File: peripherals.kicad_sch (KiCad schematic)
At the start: 23 parts, among them CN1 PJ-3059-B, CN2 PJ-3059-B, SW3 K2-1808SN-A4SW, SW4 K2-1808SN-A4SW, U48 2.54-1*4, U49 2.54-1*4, U50 LMV358IDR

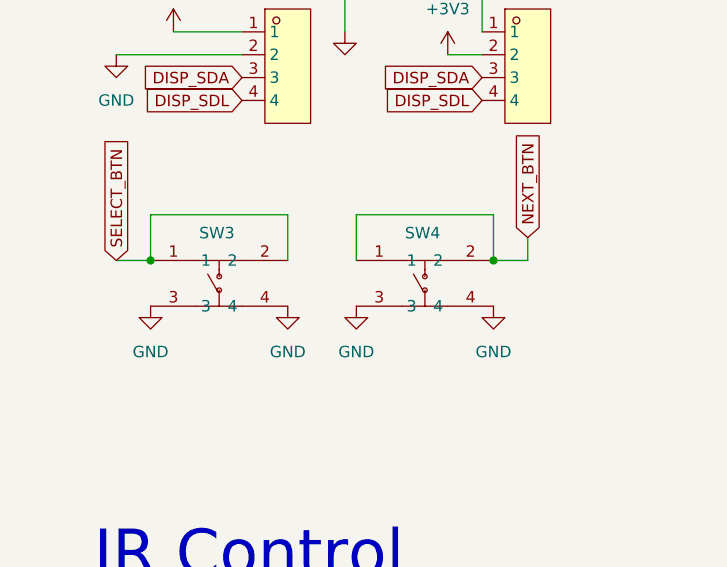
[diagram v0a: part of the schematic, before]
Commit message: Library shuffle and Fabrication Toolkit micro adjustments
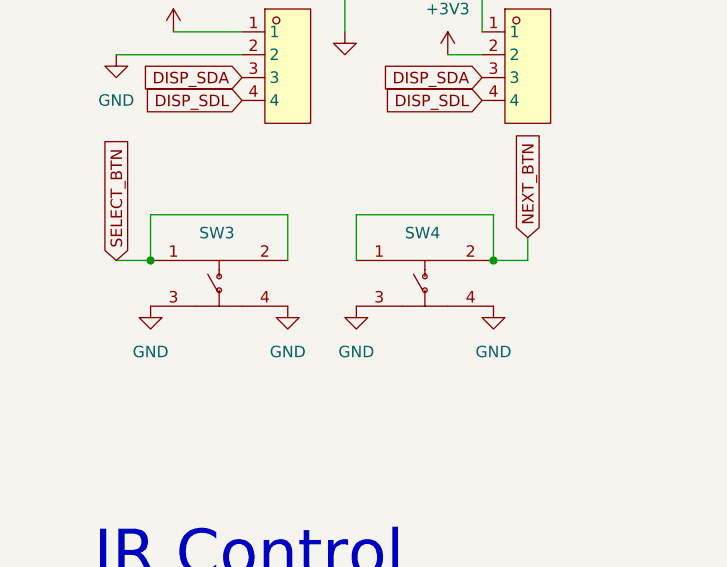
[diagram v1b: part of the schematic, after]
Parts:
- C43: footprint PCM_JLCPCB:C_0402 -> PixelBlit:C_0402; symbol PCM_JLCPCB-Capacitors:0402,1uF -> PixelBlit:0402,1uF
- C44: footprint PCM_JLCPCB:C_0402 -> PixelBlit:C_0402; symbol PCM_JLCPCB-Capacitors:0402,100nF -> PixelBlit:0402,100nF
- C45: footprint PCM_JLCPCB:C_0402 -> PixelBlit:C_0402; symbol PCM_JLCPCB-Capacitors:0402,4.7uF -> PixelBlit:0402,4.7uF
- CN1, CN2: footprint EasyEDA:AUDIO-TH_XKB_PJ-3059-B -> PixelBlit:AUDIO-TH_XKB_PJ-3059-B; symbol EasyEDA:PJ-3059-B -> PixelBlit:PJ-3059-B
- Card1: footprint EasyEDA:TF-SMD_TF-PUSH -> PixelBlit:TF-SMD_TF-PUSH; symbol EasyEDA:TFPUSH -> PixelBlit:TFPUSH
- D4, D5: footprint PCM_JLCPCB:D_SMA -> PixelBlit:D_SMA; symbol PCM_JLCPCB-Diodes:Schottky,SS14 -> PixelBlit:Schottky,SS14
- D6: footprint PCM_JLCPCB:D_0603 -> PixelBlit:D_0603; symbol PCM_JLCPCB-Diodes:LED,0603,Red -> PixelBlit:LED,0603,Red
- R57, R58, R59: footprint PCM_JLCPCB:R_0402 -> PixelBlit:R_0402; symbol PCM_JLCPCB-Resistors:0402,47kΩ -> PixelBlit:0402,47kΩ
- R60, R61: footprint PCM_JLCPCB:R_0603 -> PixelBlit:R_0603; symbol PCM_JLCPCB-Resistors:0603,1kΩ -> PixelBlit:0603,1kΩ
- R62: footprint EasyEDA:RES-ADJ-TH_3362P -> PixelBlit:RES-ADJ-TH_3362P; symbol EasyEDA:3362P-1-503LF -> PixelBlit:3362P-1-503LF
- R65: footprint PCM_JLCPCB:R_0402 -> PixelBlit:R_0402; symbol PCM_JLCPCB-Resistors:0402,1kΩ -> PixelBlit:0402,1kΩ
- R66: footprint PCM_JLCPCB:R_0402 -> PixelBlit:R_0402; symbol PCM_JLCPCB-Resistors:0402,1kΩ -> PixelBlit:0402,1kΩ_1
- R67: footprint PCM_JLCPCB:R_0402 -> PixelBlit:R_0402; symbol PCM_JLCPCB-Resistors:0402,470kΩ -> PixelBlit:0402,470kΩ
- SW3, SW4: footprint EasyEDA:KEY-SMD_4P-L4.2-W3.2-P2.20-LS5.1-TL -> PixelBlit:KEY-SMD_4P-L4.2-W3.2-P2.20-LS5.1-TL; symbol EasyEDA:K2-1808SN-A4SW -> PixelBlit:K2-1808SN-A4SW
- U48, U49: footprint EasyEDA:HDR-TH_4P-P2.54-V-M-1 -> PixelBlit:HDR-TH_4P-P2.54-V-M-1; symbol EasyEDA:2.54-1*4 -> PixelBlit:2.54-1*4
- U50: footprint EasyEDA:SOIC-8_L4.9-W3.9-P1.27-LS6.0-BL -> PixelBlit:SOIC-8_L4.9-W3.9-P1.27-LS6.0-BL; symbol EasyEDA:LMV358IDR -> PixelBlit:LMV358IDR
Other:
- moved on the sheet: SW3, SW4
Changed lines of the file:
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@@
 	)
 	(symbol
-		(lib_id "power:GND")
+		(lib_id "PixelBlit:GND")
 		(at 67.31 66.04 0)
 		(unit 1)
@@
 	)
 	(symbol
-		(lib_id "power:GND")
+		(lib_id "PixelBlit:GND")
 		(at 180.34 146.05 0)
 		(unit 1)
@@
 	)
 	(symbol
-		(lib_id "PCM_JLCPCB-Diodes:Schottky,SS14")
+		(lib_id "PixelBlit:Schottky,SS14")
 		(at 125.73 123.19 180)
 		(unit 1)
@@
 			)
 		)
-		(property "Footprint" "PCM_JLCPCB:D_SMA"
+		(property "Footprint" "PixelBlit:D_SMA"
 			(at 127.508 123.19 90)
 			(effects
@@
 	)
 	(symbol
-		(lib_id "EasyEDA:PJ-3059-B")
+		(lib_id "PixelBlit:PJ-3059-B")
 		(at 138.43 101.6 0)
 		(unit 1)
@@
 			)
 		)
-		(property "Footprint" "EasyEDA:AUDIO-TH_XKB_PJ-3059-B"
+		(property "Footprint" "PixelBlit:AUDIO-TH_XKB_PJ-3059-B"
 			(at 138.43 114.3 0)
 			(effects
@@
 	)
 	(symbol
-		(lib_id "power:GND")
+		(lib_id "PixelBlit:GND")
 		(at 54.61 119.38 0)
 		(unit 1)
@@
 	)
 	(symbol
-		(lib_id "power:GND")
+		(lib_id "PixelBlit:GND")
 		(at 44.45 66.04 0)
 		(unit 1)
@@
 	)
 	(symbol
-		(lib_id "power:GND")
+		(lib_id "PixelBlit:GND")
 		(at 82.55 66.04 0)
 		(unit 1)
@@
 	)
 	(symbol
-		(lib_id "power:GND")
+		(lib_id "PixelBlit:GND")
 		(at 40.64 38.1 0)
 		(unit 1)
@@
 	)
 	(symbol
-		(lib_id "PCM_JLCPCB-Resistors:0402,47kΩ")
+		(lib_id "PixelBlit:0402,47kΩ")
 		(at 175.26 30.48 0)
 		(unit 1)
@@
 			)
 		)
-		(property "Footprint" "PCM_JLCPCB:R_0402"
+		(property "Footprint" "PixelBlit:R_0402"
 			(at 173.482 30.48 90)
 			(effects
@@
 	)
 	(symbol
-		(lib_id "PCM_JLCPCB-Resistors:0402,47kΩ")
+		(lib_id "PixelBlit:0402,47kΩ")
 		(at 175.26 45.72 0)
 		(unit 1)
@@
 			)
 		)
-		(property "Footprint" "PCM_JLCPCB:R_0402"
+		(property "Footprint" "PixelBlit:R_0402"
 			(at 173.482 45.72 90)
 			(effects
@@
 	)
 	(symbol
-		(lib_id "EasyEDA:K2-1808SN-A4SW")
+		(lib_id "PixelBlit:K2-1808SN-A4SW")
 		(at 74.93 63.5 0)
 		(unit 1)
@@
 			)
 		)
-		(property "Footprint" "EasyEDA:KEY-SMD_4P-L4.2-W3.2-P2.20-LS5.1-TL"
+		(property "Footprint" "PixelBlit:KEY-SMD_4P-L4.2-W3.2-P2.20-LS5.1-TL"
 			(at 74.93 73.66 0)
 			(effects
@@
 	)
 	(symbol
-		(lib_id "power:+3V3")
+		(lib_id "PixelBlit:+3V3")
 		(at 46.99 35.56 0)
 		(unit 1)
@@
 	)
 	(symbol
-		(lib_id "PCM_JLCPCB-Resistors:0603,1kΩ")
+		(lib_id "PixelBlit:0603,1kΩ")
 		(at 193.04 96.52 180)
 		(unit 1)
@@
 			)
 		)
-		(property "Footprint" "PCM_JLCPCB:R_0603"
+		(property "Footprint" "PixelBlit:R_0603"
 			(at 194.818 96.52 90)
 			(effects
@@
 	)
 	(symbol
-		(lib_id "PCM_JLCPCB-Resistors:0402,1kΩ")
+		(lib_id "PixelBlit:0402,1kΩ")
 		(at 212.09 128.27 270)
 		(unit 1)
@@
 			)
 		)
-		(property "Footprint" "PCM_JLCPCB:R_0402"
+		(property "Footprint" "PixelBlit:R_0402"
 			(at 212.09 126.492 90)
 			(effects
@@
 	(symbol
 		(lib_name "0402,1kΩ_1")
-		(lib_id "PCM_JLCPCB-Resistors:0402,1kΩ")
+		(lib_id "PixelBlit:0402,1kΩ_1")
 		(at 158.75 119.38 0)
 		(unit 1)
@@
 			)
 		)
-		(property "Footprint" "PCM_JLCPCB:R_0402"
+		(property "Footprint" "PixelBlit:R_0402"
 			(at 156.972 119.38 90)
 			(effects
@@
 	)
 	(symbol
-		(lib_id "PCM_JLCPCB-Diodes:LED,0603,Red")
+		(lib_id "PixelBlit:LED,0603,Red")
 		(at 222.25 128.27 90)
 		(unit 1)
@@
 			)
 		)
-		(property "Footprint" "PCM_JLCPCB:D_0603"
+		(property "Footprint" "PixelBlit:D_0603"
 			(at 222.25 130.048 90)
 			(effects
@@
 	)
 	(symbol
-		(lib_id "PCM_JLCPCB-Capacitors:0402,4.7uF")
+		(lib_id "PixelBlit:0402,4.7uF")
 		(at 240.03 121.92 0)
 		(unit 1)
@@
 			)
 		)
-		(property "Footprint" "PCM_JLCPCB:C_0402"
+		(property "Footprint" "PixelBlit:C_0402"
 			(at 238.252 121.92 90)
 			(effects
@@
 	)
 	(symbol
-		(lib_id "power:+5V")
+		(lib_id "PixelBlit:+5V")
 		(at 54.61 105.41 0)
 		(unit 1)
@@
 	)
 	(symbol
-		(lib_id "EasyEDA:2.54-1*4")
+		(lib_id "PixelBlit:2.54-1*4")
 		(at 86.36 39.37 0)
 		(unit 1)
@@
 			)
 		)
-		(property "Footprint" "EasyEDA:HDR-TH_4P-P2.54-V-M-1"
+		(property "Footprint" "PixelBlit:HDR-TH_4P-P2.54-V-M-1"
 			(at 86.36 50.8 0)
 			(effects
@@
 	)
 	(symbol
-		(lib_id "power:+5V")
+		(lib_id "PixelBlit:+5V")
 		(at 125.73 120.65 0)
 		(unit 1)
@@
 	)
 	(symbol
-		(lib_id "EasyEDA:TFPUSH")
+		(lib_id "PixelBlit:TFPUSH")
 		(at 190.5 54.61 0)
 		(unit 1)
@@
 			)
 		)
-		(property "Footprint" "EasyEDA:TF-SMD_TF-PUSH"
+		(property "Footprint" "PixelBlit:TF-SMD_TF-PUSH"
 			(at 190.5 77.47 0)
 			(effects
@@
 	)
 	(symbol
-		(lib_id "PCM_JLCPCB-Resistors:0603,1kΩ")
+		(lib_id "PixelBlit:0603,1kΩ")
 		(at 152.4 104.14 90)
 		(unit 1)
@@
 			)
 		)
-		(property "Footprint" "PCM_JLCPCB:R_0603"
+		(property "Footprint" "PixelBlit:R_0603"
 			(at 152.4 105.918 90)
 			(effects
@@
 	)
 	(symbol
-		(lib_id "power:+5V")
+		(lib_id "PixelBlit:+5V")
 		(at 246.38 113.03 0)
 		(unit 1)
@@
 	)
 	(symbol
-		(lib_id "power:GND")
+		(lib_id "PixelBlit:GND")
 		(at 198.12 73.66 0)
 		(unit 1)
@@
 	)
 	(symbol
-		(lib_id "power:GND")
+		(lib_id "PixelBlit:GND")
 		(at 217.17 101.6 0)
 		(unit 1)
@@
 	)
 	(symbol
-		(lib_id "power:GND")
+		(lib_id "PixelBlit:GND")
 		(at 59.69 66.04 0)
 		(unit 1)
@@
 	)
 	(symbol
-		(lib_id "power:+5V")
+		(lib_id "PixelBlit:+5V")
 		(at 152.4 52.07 0)
 		(unit 1)
@@
 	)
 	(symbol
-		(lib_id "PCM_JLCPCB-Resistors:0402,47kΩ")
+		(lib_id "PixelBlit:0402,47kΩ")
 		(at 175.26 63.5 0)
 		(unit 1)
@@
 			)
 		)
-		(property "Footprint" "PCM_JLCPCB:R_0402"
+		(property "Footprint" "PixelBlit:R_0402"
 			(at 173.482 63.5 90)
 			(effects
@@
 	)
 	(symbol
-		(lib_id "PCM_JLCPCB-Resistors:0402,470kΩ")
+		(lib_id "PixelBlit:0402,470kΩ")
 		(at 158.75 97.79 0)
 		(unit 1)
@@
 			)
 		)
-		(property "Footprint" "PCM_JLCPCB:R_0402"
+		(property "Footprint" "PixelBlit:R_0402"
 			(at 156.972 97.79 90)
 			(effects
@@
 	)
 	(symbol
-		(lib_id "power:GND")
+		(lib_id "PixelBlit:GND")
 		(at 158.75 57.15 0)
 		(unit 1)
@@
 	)
 	(symbol
-		(lib_id "PCM_JLCPCB-Capacitors:0402,1uF")
+		(lib_id "PixelBlit:0402,1uF")
 		(at 168.91 104.14 90)
 		(unit 1)
@@
 			)
 		)
-		(property "Footprint" "PCM_JLCPCB:C_0402"
+		(property "Footprint" "PixelBlit:C_0402"
 			(at 168.91 105.918 90)
 			(effects
@@
 	)
 	(symbol
-		(lib_id "EasyEDA:2.54-1*4")
+		(lib_id "PixelBlit:2.54-1*4")
 		(at 59.69 39.37 0)
 		(unit 1)
@@
 			)
 		)
-		(property "Footprint" "EasyEDA:HDR-TH_4P-P2.54-V-M-1"
+		(property "Footprint" "PixelBlit:HDR-TH_4P-P2.54-V-M-1"
 			(at 59.69 50.8 0)
 			(effects
@@
 	)
 	(symbol
-		(lib_id "EasyEDA:PJ-3059-B")
+		(lib_id "PixelBlit:PJ-3059-B")
 		(at 57.15 113.03 180)
 		(unit 1)
@@
 			)
 		)
-		(property "Footprint" "EasyEDA:AUDIO-TH_XKB_PJ-3059-B"
+		(property "Footprint" "PixelBlit:AUDIO-TH_XKB_PJ-3059-B"
 			(at 57.15 100.33 0)
 			(effects
@@
 	)
 	(symbol
-		(lib_id "EasyEDA:3362P-1-503LF")
+		(lib_id "PixelBlit:3362P-1-503LF")
 		(at 191.77 110.49 0)
 		(unit 1)
@@
 			)
 		)
-		(property "Footprint" "EasyEDA:RES-ADJ-TH_3362P"
+		(property "Footprint" "PixelBlit:RES-ADJ-TH_3362P"
 			(at 191.77 123.19 0)
 			(effects
@@
 	)
 	(symbol
-		(lib_id "power:GND")
+		(lib_id "PixelBlit:GND")
 		(at 66.04 35.56 0)
 		(unit 1)
@@
 	)
 	(symbol
-		(lib_id "power:+3V3")
+		(lib_id "PixelBlit:+3V3")
 		(at 77.47 38.1 0)
 		(unit 1)
@@
 	)
 	(symbol
-		(lib_id "PCM_JLCPCB-Diodes:Schottky,SS14")
+		(lib_id "PixelBlit:Schottky,SS14")
 		(at 144.78 104.14 90)
 		(unit 1)
@@
 			)
 		)
-		(property "Footprint" "PCM_JLCPCB:D_SMA"
+		(property "Footprint" "PixelBlit:D_SMA"
 			(at 144.78 105.918 90)
 			(effects
@@
 	)
 	(symbol
-		(lib_id "EasyEDA:K2-1808SN-A4SW")
+		(lib_id "PixelBlit:K2-1808SN-A4SW")
 		(at 52.07 63.5 0)
 		(unit 1)
@@
 			)
 		)
-		(property "Footprint" "EasyEDA:KEY-SMD_4P-L4.2-W3.2-P2.20-LS5.1-TL"
+		(property "Footprint" "PixelBlit:KEY-SMD_4P-L4.2-W3.2-P2.20-LS5.1-TL"
 			(at 52.07 73.66 0)
 			(effects
@@
 	)
 	(symbol
-		(lib_id "PCM_JLCPCB-Capacitors:0402,100nF")
+		(lib_id "PixelBlit:0402,100nF")
 		(at 229.87 121.92 0)
 		(unit 1)
@@
 			)
 		)
-		(property "Footprint" "PCM_JLCPCB:C_0402"
+		(property "Footprint" "PixelBlit:C_0402"
 			(at 228.092 121.92 90)
 			(effects
@@
 	)
 	(symbol
-		(lib_id "EasyEDA:LMV358IDR")
+		(lib_id "PixelBlit:LMV358IDR")
 		(at 180.34 132.08 0)
 		(unit 1)
@@
 			)
 		)
-		(property "Footprint" "EasyEDA:SOIC-8_L4.9-W3.9-P1.27-LS6.0-BL"
+		(property "Footprint" "PixelBlit:SOIC-8_L4.9-W3.9-P1.27-LS6.0-BL"
 			(at 180.34 143.51 0)
 			(effects

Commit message: Working on errata
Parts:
- removed C43: 1uF, PixelBlit:C_0402, symbol PixelBlit:0402,1uF
- removed C44: 100nF, PixelBlit:C_0402, symbol PixelBlit:0402,100nF
- removed C45: 4.7uF, PixelBlit:C_0402, symbol PixelBlit:0402,4.7uF
- removed CN2: PJ-3059-B, PixelBlit:AUDIO-TH_XKB_PJ-3059-B, symbol PixelBlit:PJ-3059-B
- removed D4, D5: SS14, PixelBlit:D_SMA, symbol PixelBlit:Schottky,SS14
- removed D6: Red, PixelBlit:D_0603, symbol PixelBlit:LED,0603,Red
- removed R60, R61: 1kΩ, PixelBlit:R_0603, symbol PixelBlit:0603,1kΩ
- removed R62: 3362P-1-503LF, PixelBlit:RES-ADJ-TH_3362P, symbol PixelBlit:3362P-1-503LF
- removed R65: 1kΩ, PixelBlit:R_0402, symbol PixelBlit:0402,1kΩ
- removed R66: 1kΩ, PixelBlit:R_0402, symbol PixelBlit:0402,1kΩ_1
- removed R67: 470kΩ, PixelBlit:R_0402, symbol PixelBlit:0402,470kΩ
- removed SW3, SW4: K2-1808SN-A4SW, PixelBlit:KEY-SMD_4P-L4.2-W3.2-P2.20-LS5.1-TL, symbol PixelBlit:K2-1808SN-A4SW
- removed U48, U49: 2.54-1*4, PixelBlit:HDR-TH_4P-P2.54-V-M-1, symbol PixelBlit:2.54-1*4
- removed U50: LMV358IDR, PixelBlit:SOIC-8_L4.9-W3.9-P1.27-LS6.0-BL, symbol PixelBlit:LMV358IDR
- added J39: PZ2.54-1*9, EasyEDA:HDR-TH_9P-P2.54-V-M, symbol EasyEDA:PZ2.54-1*9
- added R2: 100Ω, PCM_JLCPCB:R_0603, symbol PCM_JLCPCB-Resistors:0603,100Ω
- added SW2: SS-22D03-G040, EasyEDA:SW-TH_SS-22D03-G4, symbol EasyEDA:SS-22D03-G040
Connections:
- net +3V3: now also J39.1
- net +5V: now also R2.1; no longer CN1.3
- net DISP_SDA: now also J39.8
- net GND: now also J39.2
- net IR_IN: now also SW2.3, SW2.4; no longer CN1.4
- new net: R2.2, SW2.1, SW2.6
- new net: CN1.3, SW2.2
- new net: CN1.4, SW2.5
- new net BAK: J39.3
- new net DISP_SCL: J39.7
- new net PSH: J39.6
- new net TRA: J39.5
- new net TRB: J39.4
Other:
- note added: "DPDT switch swaps IR_IN and 5V As devices are not standard"
- note added: "To prevent shorting the 5V rail on insertion The transceiver doesn't draw much current, and runs down to 3V anyway"
- note removed: "Adjustable Pot for Amplifier gain. Adjust until the LED varies across a good level of brightness. Between unity and 51x"
- note removed: "Audio In"
- note removed: "Must be a rail-to-rail op amp as the signal is small. 1Vpp audio in, so that's 500mV after the diode, but the diode drops 200mV. So best case I've only got 300mV. Times 11 gets me back to 3.3V"
- note removed: "RC cutoff of about 160Hz. This preserves the beat and overall amplitude"
- moved on the sheet: CN1
